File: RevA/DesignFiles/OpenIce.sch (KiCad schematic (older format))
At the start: 1 part, among them U1 ICE40HX1K-TQ144

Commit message: finshed naming pins in multi unit
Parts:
- removed U1: ICE40HX1K-TQ144, ICE40HX1K-TQ144:QFP50P2200X2200X160-144N, symbol ICE40HX1K-TQ144
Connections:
- wire segments 1 -> 0
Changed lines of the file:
@@
 EESchema Schematic File Version 2
+LIBS:OpenIce-rescue
 LIBS:power
 LIBS:device
@@
 Comment4 ""
 $EndDescr
-$Comp
-L ICE40HX1K-TQ144 U1
-U 1 1 57EEA3B3
-P 4900 3150
-F 0 "U1" H 2900 4950 50  0000 L CNN
-F 1 "ICE40HX1K-TQ144" H 2900 250 50  0000 L CNN
-F 2 "ICE40HX1K-TQ144:QFP50P2200X2200X160-144N" H 4900 3150 50  0001 L CNN
-F 3 "HX Series 1280 LUTs 95 I/O 64 kBit RAM 1.2 V Surface Mount FPGA - TQFP-144" H 4900 3150 50  0001 L CNN
-F 4 "Good" H 4900 3150 50  0001 L CNN "Availability"
-F 5 "5.04 USD" H 4900 3150 50  0001 L CNN "Price"
-F 6 "TQFP-144 Lattice Semiconductor" H 4900 3150 50  0001 L CNN "Package"
-F 7 "Lattice Semiconductor" H 4900 3150 50  0001 L CNN "MF"
-F 8 "ICE40HX1K-TQ144" H 4900 3150 50  0001 L CNN "MP"
-	1    4900 3150
-	1    0    0    -1
-$EndComp
-Wire Wire Line
-	3650 4100 4450 4100
 $Sheet
 S 7900 2550 1450 600

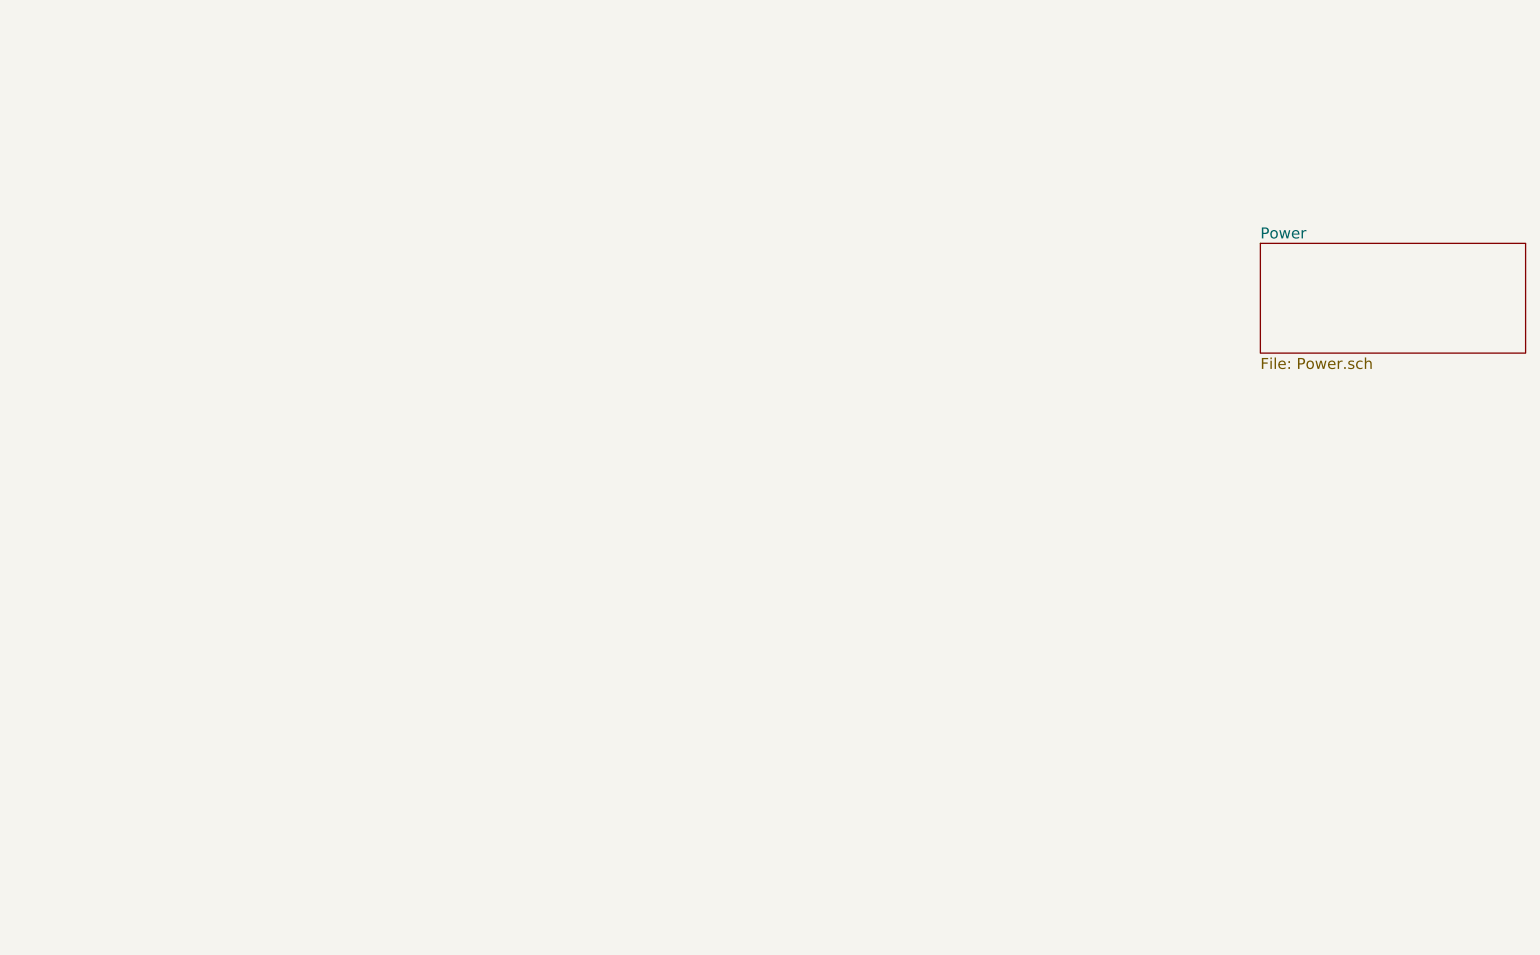
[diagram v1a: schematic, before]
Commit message: placed power block and usb connector
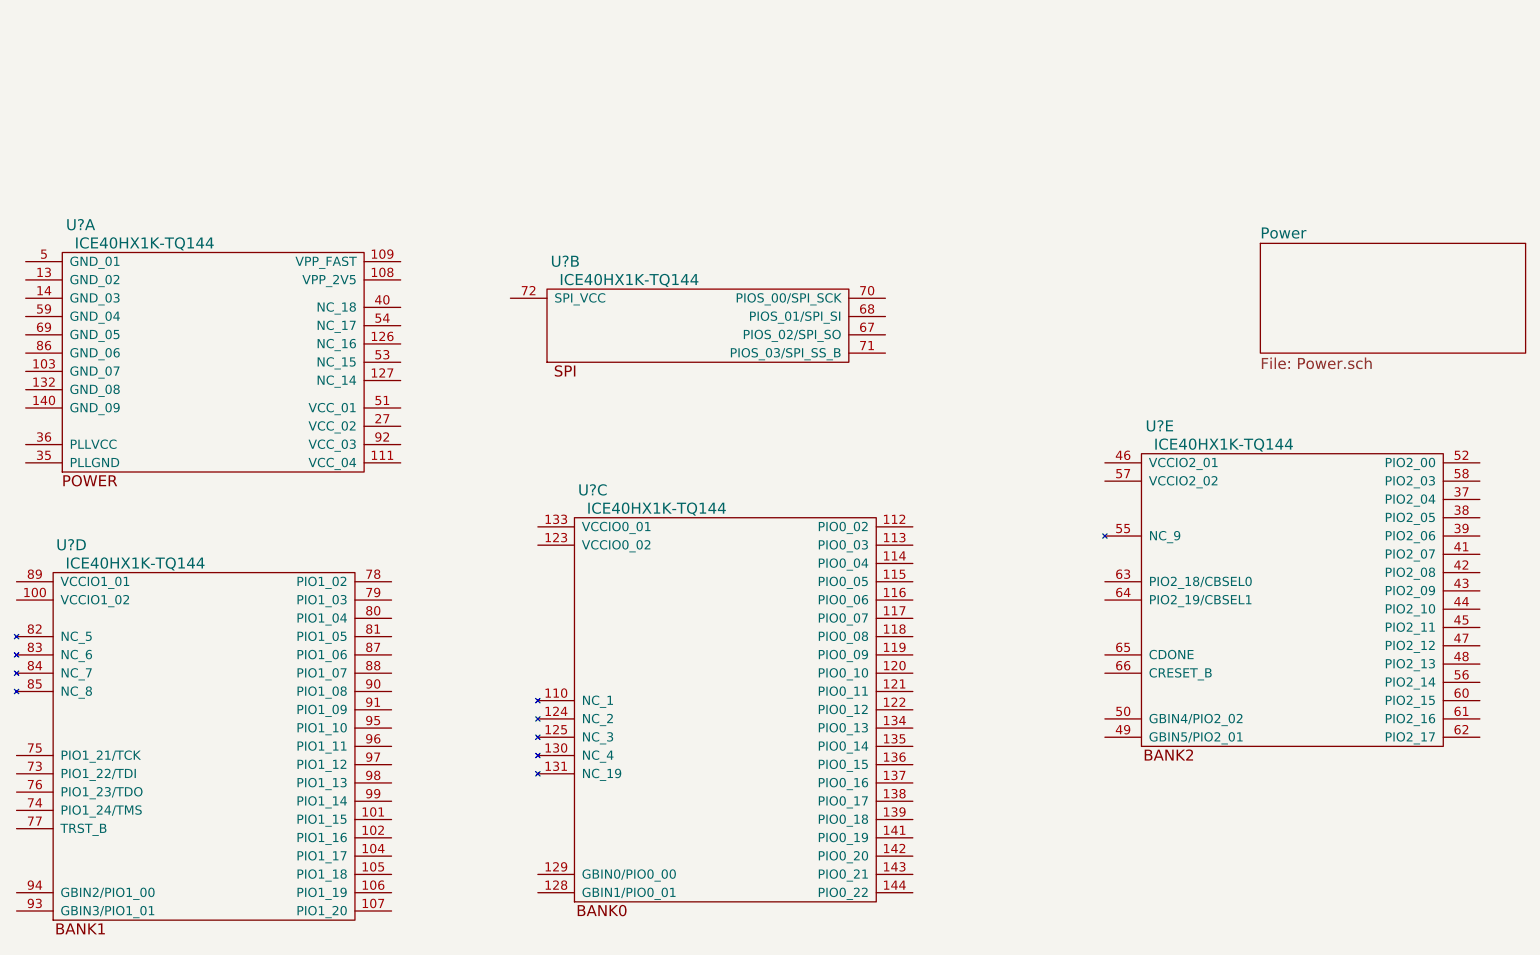
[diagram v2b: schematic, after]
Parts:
- added U? (x5): ICE40HX1K-TQ144, symbol ICE40HX1K-TQ144
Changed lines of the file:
@@
 F1 "Power.sch" 60
 $EndSheet
+$Comp
+L ICE40HX1K-TQ144 U?
+U 1 1 57FD4B3E
+P 1150 2600
+F 0 "U?" H 1450 2750 60  0000 C CNN
+F 1 "ICE40HX1K-TQ144" H 1800 2650 60  0000 C CNN
+F 2 "" H 1150 1850 60  0000 C CNN
+F 3 "" H 1150 1850 60  0000 C CNN
+	1    1150 2600
+	1    0    0    -1
+$EndComp
+$Comp
+L ICE40HX1K-TQ144 U?
+U 2 1 57FD4B8D
+P 3800 2800
+F 0 "U?" H 4100 2950 60  0000 C CNN
+F 1 "ICE40HX1K-TQ144" H 4450 2850 60  0000 C CNN
+F 2 "" H 3800 2050 60  0000 C CNN
+F 3 "" H 3800 2050 60  0000 C CNN
+	2    3800 2800
+	1    0    0    -1
+$EndComp
+$Comp
+L ICE40HX1K-TQ144 U?
+U 3 1 57FD4BD6
+P 3950 4050
+F 0 "U?" H 4250 4200 60  0000 C CNN
+F 1 "ICE40HX1K-TQ144" H 4600 4100 60  0000 C CNN
+F 2 "" H 3950 3300 60  0000 C CNN
+F 3 "" H 3950 3300 60  0000 C CNN
+	3    3950 4050
+	1    0    0    -1
+$EndComp
+$Comp
+L ICE40HX1K-TQ144 U?
+U 4 1 57FD4C41
+P 1100 4350
+F 0 "U?" H 1400 4500 60  0000 C CNN
+F 1 "ICE40HX1K-TQ144" H 1750 4400 60  0000 C CNN
+F 2 "" H 1100 3600 60  0000 C CNN
+F 3 "" H 1100 3600 60  0000 C CNN
+	4    1100 4350
+	1    0    0    -1
+$EndComp
+$Comp
+L ICE40HX1K-TQ144 U?
+U 5 1 57FD4C9C
+P 7050 3700
+F 0 "U?" H 7350 3850 60  0000 C CNN
+F 1 "ICE40HX1K-TQ144" H 7700 3750 60  0000 C CNN
+F 2 "" H 7050 2950 60  0000 C CNN
+F 3 "" H 7050 2950 60  0000 C CNN
+	5    7050 3700
+	1    0    0    -1
+$EndComp
 $EndSCHEMATC
